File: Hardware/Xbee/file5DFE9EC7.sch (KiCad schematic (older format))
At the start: 36 parts, among them J1 Alimentación, J2 Raspberry, J3 Pines 1, J4 Pines 2, J5 Programación, J6 Entrada, J7 Salida, K1 SANYOU_SRD_Form_C, Q1 2N7002, Q2 AP2300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

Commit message: Sheets-Text
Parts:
- removed D1: Blue Assoc-RSSI, LED_SMD:LED_0805_2012Metric, symbol Xbee-rescue:LED_ALT-Device
- removed D3: Zener 5V, Diode_SMD:D_SOT-23_ANK, symbol Xbee-rescue:D_Zener_ALT-Device
- removed D4: 1N4007WS, Diode_SMD:D_SOD-323_HandSoldering, symbol Xbee-rescue:1N4007-Diode
- removed D5: LED ON, Connector_PinSocket_2.54mm:PinSocket_1x02_P2.54mm_Vertical, symbol Xbee-rescue:LED_ALT-Device
- removed D6: LED Batería, Connector_PinSocket_2.54mm:PinSocket_1x02_P2.54mm_Vertical, symbol Xbee-rescue:LED_ALT-Device
- removed D7: LED Green Salida, LED_SMD:LED_0805_2012Metric, symbol Xbee-rescue:LED_ALT-Device
- removed J1: Alimentación, TerminalBlock:TerminalBlock_bornier-2_P5.08mm, symbol Xbee-rescue:Screw_Terminal_01x02-Connector
- removed J2: Raspberry, Connector_PinHeader_2.54mm:PinHeader_1x05_P2.54mm_Vertical, symbol Xbee-rescue:Conn_01x05-Connector_Generic
- removed J3: Pines 1, Connector_PinSocket_2.54mm:PinSocket_1x10_P2.54mm_Vertical, symbol Xbee-rescue:Conn_01x10-Connector_Generic
- removed J4: Pines 2, Connector_PinSocket_2.54mm:PinSocket_1x10_P2.54mm_Vertical, symbol Xbee-rescue:Conn_01x10-Connector_Generic
- removed J5: Programación, Connector_PinHeader_2.54mm:PinHeader_2x05_P2.54mm_Horizontal, symbol Xbee-rescue:Conn_02x05_Counter_Clockwise-Connector_Generic
- removed J6: Entrada, TerminalBlock:TerminalBlock_bornier-2_P5.08mm, symbol Xbee-rescue:Screw_Terminal_01x02-Connector
- removed J7: Salida, TerminalBlock:TerminalBlock_bornier-2_P5.08mm, symbol Xbee-rescue:Screw_Terminal_01x02-Connector
- removed JP1: Assoc-RSSI, Connector_PinHeader_2.54mm:PinHeader_1x03_P2.54mm_Vertical, symbol Xbee-rescue:Jumper_3_Open-Jumper
- removed JP2: Loopback, Connector_PinHeader_2.54mm:PinHeader_1x02_P2.54mm_Vertical, symbol Xbee-rescue:Jumper_2_Open-Jumper
- removed JP3: DIO2 E/S, Connector_PinHeader_2.54mm:PinHeader_1x03_P2.54mm_Vertical, symbol Xbee-rescue:Jumper_3_Open-Jumper
- removed JP4: Estado Batería, Connector_PinHeader_2.54mm:PinHeader_1x02_P2.54mm_Vertical, symbol Xbee-rescue:Jumper_2_Open-Jumper
- removed K1: SANYOU_SRD_Form_C, Relay_THT:Relay_SPDT_SANYOU_SRD_Series_Form_C, symbol Relay:SANYOU_SRD_Form_C
- removed Q1: 2N7002, Package_TO_SOT_SMD:SOT-23, symbol Transistor_FET:2N7002
- removed Q2: AP2300, Package_TO_SOT_SMD:SOT-23, symbol Transistor_FET:2N7002
- removed R1, R5, R9: 330, Resistor_SMD:R_0805_2012Metric_Pad1.15x1.40mm_HandSolder, symbol Xbee-rescue:R-Device
- removed R10, R6, R8: 10k, Resistor_SMD:R_0805_2012Metric_Pad1.15x1.40mm_HandSolder, symbol Xbee-rescue:R-Device
- removed R11, R12: 560, Resistor_SMD:R_0805_2012Metric_Pad1.15x1.40mm_HandSolder, symbol Xbee-rescue:R-Device
- removed R13: 4k7, Resistor_SMD:R_0805_2012Metric_Pad1.15x1.40mm_HandSolder, symbol Xbee-rescue:R-Device
- removed R7: 3.3k, Resistor_SMD:R_0805_2012Metric_Pad1.15x1.40mm_HandSolder, symbol Xbee-rescue:R-Device
- removed RV1, RV2: 10k, Potentiometer_THT:Potentiometer_Bourns_3386C_Horizontal, symbol Xbee-rescue:R_POT-Device
- removed SW1: Reset, Button_Switch_THT:SW_TH_Tactile_Omron_B3F-10xx, symbol Xbee-rescue:SW_Push_Dual-Switch
- removed SW2: Comm., Button_Switch_THT:SW_TH_Tactile_Omron_B3F-10xx, symbol Xbee-rescue:SW_Push_Dual-Switch
- removed U2: Xbee, XBP24CZ7PITB003:DIP2200W51P200L3294H279Q20P, symbol Xbee-rescue:XBP24CZ7PITB003-XBP24CZ7PITB003
- removed U3: LM358, Package_SO:SO-8_3.9x4.9mm_P1.27mm, symbol Xbee-rescue:LM358-Amplifier_Operational
- added C1, C2: 1u, Capacitor_SMD:C_0805_2012Metric, symbol Xbee-rescue:CP1-Device
- added U1: AZ1117-3.3, Package_TO_SOT_SMD:SOT-223-3_TabPin2, symbol Regulator_Linear:AZ1117-3.3
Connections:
- net GNDREF: now also C1.2, C2.2, U1.1 (GND)
- new net Entrada-12V: C1.1, U1.3 (VI)
- new net Salida-3.3V: C2.1, U1.2 (VO)
- no-connect marks 6 -> 0
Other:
- note added: "Regulador-3.3V"
- note removed: "Borneras-Entrada-Salida"
- note removed: "Botones"
- note removed: "Circuito-Salida"
- note removed: "Estado-Batería"
- note removed: "Jumper-Prog"
- note removed: "LED's Indicadores"
- note removed: "Lectura-Estado-Bateria"

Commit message: Battery Charger
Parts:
- added D2, D9: D_Schottky_ALT, symbol Device:D_Schottky_ALT
- added D8: D_ALT, symbol Device:D_ALT
- added Q3: DMP3099L-7, Package_TO_SOT_SMD:SOT-23, symbol Transistor_FET:DMP3013SFV
- added R2: 100, symbol Device:R
- added R3: 10k, symbol Device:R
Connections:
- net labels added: +12V, Bat+, CargaBat, Vin+
- wire segments 9 -> 23
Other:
- note added: "Cargador de batería"
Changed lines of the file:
@@
 EndData
 $EndBitmap
+Text HLabel 6000 1350 1    50   Input ~ 0
+Vin+
+Text HLabel 4700 2250 0    50   Input ~ 0
+Bat+
+$Comp
+L Device:D_Schottky_ALT D2
+U 1 1 5D952A15
+P 4750 1500
+F 0 "D2" H 4750 1716 50  0000 C CNN
+F 1 "D_Schottky_ALT" H 4750 1625 50  0000 C CNN
+F 2 "" H 4750 1500 50  0001 C CNN
+F 3 "~" H 4750 1500 50  0001 C CNN
+	1    4750 1500
+	0    -1   -1   0
+$EndComp
+$Comp
+L Device:D_ALT D8
+U 1 1 5D952EF8
+P 5800 2250
+F 0 "D8" H 5800 2034 50  0000 C CNN
+F 1 "D_ALT" H 5800 2125 50  0000 C CNN
+F 2 "" H 5800 2250 50  0001 C CNN
+F 3 "~" H 5800 2250 50  0001 C CNN
+	1    5800 2250
+	-1   0    0    1
+$EndComp
+$Comp
+L Device:R R3
+U 1 1 5D9533C4
+P 5600 1500
+F 0 "R3" H 5670 1546 50  0000 L CNN
+F 1 "10k" H 5670 1455 50  0000 L CNN
+F 2 "" V 5530 1500 50  0001 C CNN
+F 3 "~" H 5600 1500 50  0001 C CNN
+	1    5600 1500
+	1    0    0    -1
+$EndComp
+Wire Wire Line
+	5300 1350 5600 1350
+Wire Wire Line
+	5100 1650 5400 1650
+Wire Wire Line
+	6000 1350 5600 1350
+Connection ~ 5600 1350
+$Comp
+L Device:D_Schottky_ALT D9
+U 1 1 5D9575F1
+P 6000 1750
+F 0 "D9" V 6046 1671 50  0000 R CNN
+F 1 "D_Schottky_ALT" V 5955 1671 50  0000 R CNN
+F 2 "" H 6000 1750 50  0001 C CNN
+F 3 "~" H 6000 1750 50  0001 C CNN
+	1    6000 1750
+	0    -1   -1   0
+$EndComp
+Wire Wire Line
+	6000 1600 6000 1350
+$Comp
+L power:+12V #PWR0103
+U 1 1 5D9587BC
+P 6250 2250
+F 0 "#PWR0103" H 6250 2100 50  0001 C CNN
+F 1 "+12V" H 6265 2423 50  0000 C CNN
+F 2 "" H 6250 2250 50  0001 C CNN
+F 3 "" H 6250 2250 50  0001 C CNN
+	1    6250 2250
+	1    0    0    -1
+$EndComp
+$Comp
+L Device:R R2
+U 1 1 5D95A68D
+P 4750 1900
+F 0 "R2" V 4543 1900 50  0000 C CNN
+F 1 "100" V 4634 1900 50  0000 C CNN
+F 2 "" V 4680 1900 50  0001 C CNN
+F 3 "~" H 4750 1900 50  0001 C CNN
+	1    4750 1900
+	1    0    0    -1
+$EndComp
+Wire Wire Line
+	6000 1900 6000 2250
+Wire Wire Line
+	5950 2250 6000 2250
+Connection ~ 6000 2250
+Wire Wire Line
+	6000 2250 6250 2250
+Wire Wire Line
+	4750 1350 4900 1350
+Wire Wire Line
+	4750 1650 4750 1750
+Wire Wire Line
+	4750 2050 4750 2250
+Wire Wire Line
+	4750 2250 5650 2250
+Wire Wire Line
+	4700 2250 4750 2250
+Connection ~ 4750 2250
+Text HLabel 5400 1950 0    50   Input ~ 0
+CargaBat
+Wire Wire Line
+	5400 1950 5400 1650
+Connection ~ 5400 1650
+Wire Wire Line
+	5400 1650 5600 1650
+Text Notes 4800 950  0    79   ~ 0
+Cargador de batería
+$Comp
+L Transistor_FET:DMP3013SFV Q3
+U 1 1 5DAEF0EF
+P 5100 1450
+F 0 "Q3" V 5443 1450 50  0000 C CNN
+F 1 "DMP3099L-7" V 5352 1450 50  0000 C CNN
+F 2 "Package_TO_SOT_SMD:SOT-23" H 5300 1375 50  0001 L CIN
+F 3 "https://www.diodes.com/assets/Datasheets/DMP3013SFV.pdf" V 5100 1450 50  0001 L CNN
+	1    5100 1450
+	0    -1   -1   0
+$EndComp
 $EndSCHEMATC

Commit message: Added Diodes Footprints
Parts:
- D2, D9: value D_Schottky_ALT -> DSU24; footprint (none) -> Diode_SMD:D_SOD-123
- D8: value D_ALT -> DSK26; footprint (none) -> Diode_SMD:D_SOD-123F
- R2: footprint (none) -> Resistor_SMD:R_2512_6332Metric_Pad1.52x3.35mm_HandSolder
- R3: footprint (none) -> Resistor_SMD:R_0805_2012Metric_Pad1.15x1.40mm_HandSolder
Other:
- moved on the sheet: D2, D8, D9, R2, R3
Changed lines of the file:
@@
 EndData
 $EndBitmap
-Text HLabel 6000 1350 1    50   Input ~ 0
+Text HLabel 5850 1450 1    50   Input ~ 0
 Vin+
-Text HLabel 4700 2250 0    50   Input ~ 0
+Text HLabel 4550 2350 0    50   Input ~ 0
 Bat+
 $Comp
 L Device:D_Schottky_ALT D2
 U 1 1 5D952A15
-P 4750 1500
-F 0 "D2" H 4750 1716 50  0000 C CNN
-F 1 "D_Schottky_ALT" H 4750 1625 50  0000 C CNN
-F 2 "" H 4750 1500 50  0001 C CNN
-F 3 "~" H 4750 1500 50  0001 C CNN
-	1    4750 1500
+P 4600 1600
+F 0 "D2" H 4600 1816 50  0000 C CNN
+F 1 "DSU24" H 4600 1725 50  0000 C CNN
+F 2 "Diode_SMD:D_SOD-123" H 4600 1600 50  0001 C CNN
+F 3 "~" H 4600 1600 50  0001 C CNN
+	1    4600 1600
 	0    -1   -1   0
 $EndComp
@@
 L Device:D_ALT D8
 U 1 1 5D952EF8
-P 5800 2250
-F 0 "D8" H 5800 2034 50  0000 C CNN
-F 1 "D_ALT" H 5800 2125 50  0000 C CNN
-F 2 "" H 5800 2250 50  0001 C CNN
-F 3 "~" H 5800 2250 50  0001 C CNN
-	1    5800 2250
+P 5650 2350
+F 0 "D8" H 5650 2134 50  0000 C CNN
+F 1 "DSK26" H 5650 2225 50  0000 C CNN
+F 2 "Diode_SMD:D_SOD-123F" H 5650 2350 50  0001 C CNN
+F 3 "~" H 5650 2350 50  0001 C CNN
+	1    5650 2350
 	-1   0    0    1
 $EndComp
@@
 L Device:R R3
 U 1 1 5D9533C4
-P 5600 1500
-F 0 "R3" H 5670 1546 50  0000 L CNN
-F 1 "10k" H 5670 1455 50  0000 L CNN
-F 2 "" V 5530 1500 50  0001 C CNN
-F 3 "~" H 5600 1500 50  0001 C CNN
-	1    5600 1500
+P 5450 1600
+F 0 "R3" H 5520 1646 50  0000 L CNN
+F 1 "10k" H 5520 1555 50  0000 L CNN
+F 2 "Resistor_SMD:R_0805_2012Metric_Pad1.15x1.40mm_HandSolder" V 5380 1600 50  0001 C CNN
+F 3 "~" H 5450 1600 50  0001 C CNN
+	1    5450 1600
 	1    0    0    -1
 $EndComp
 Wire Wire Line
-	5300 1350 5600 1350
+	5150 1450 5450 1450
 Wire Wire Line
-	5100 1650 5400 1650
+	4950 1750 5250 1750
 Wire Wire Line
-	6000 1350 5600 1350
-Connection ~ 5600 1350
+	5850 1450 5450 1450
+Connection ~ 5450 1450
 $Comp
 L Device:D_Schottky_ALT D9
 U 1 1 5D9575F1
-P 6000 1750
-F 0 "D9" V 6046 1671 50  0000 R CNN
-F 1 "D_Schottky_ALT" V 5955 1671 50  0000 R CNN
-F 2 "" H 6000 1750 50  0001 C CNN
-F 3 "~" H 6000 1750 50  0001 C CNN
-	1    6000 1750
+P 5850 1850
+F 0 "D9" V 5896 1771 50  0000 R CNN
+F 1 "DSU24" V 5805 1771 50  0000 R CNN
+F 2 "Diode_SMD:D_SOD-123" H 5850 1850 50  0001 C CNN
+F 3 "~" H 5850 1850 50  0001 C CNN
+	1    5850 1850
 	0    -1   -1   0
 $EndComp
 Wire Wire Line
-	6000 1600 6000 1350
+	5850 1700 5850 1450
 $Comp
 L power:+12V #PWR0103
 U 1 1 5D9587BC
-P 6250 2250
-F 0 "#PWR0103" H 6250 2100 50  0001 C CNN
-F 1 "+12V" H 6265 2423 50  0000 C CNN
-F 2 "" H 6250 2250 50  0001 C CNN
-F 3 "" H 6250 2250 50  0001 C CNN
-	1    6250 2250
+P 6100 2350
+F 0 "#PWR0103" H 6100 2200 50  0001 C CNN
+F 1 "+12V" H 6115 2523 50  0000 C CNN
+F 2 "" H 6100 2350 50  0001 C CNN
+F 3 "" H 6100 2350 50  0001 C CNN
+	1    6100 2350
 	1    0    0    -1
 $EndComp
@@
 L Device:R R2
 U 1 1 5D95A68D
-P 4750 1900
-F 0 "R2" V 4543 1900 50  0000 C CNN
-F 1 "100" V 4634 1900 50  0000 C CNN
-F 2 "" V 4680 1900 50  0001 C CNN
-F 3 "~" H 4750 1900 50  0001 C CNN
-	1    4750 1900
+P 4600 2000
+F 0 "R2" V 4393 2000 50  0000 C CNN
+F 1 "100" V 4484 2000 50  0000 C CNN
+F 2 "Resistor_SMD:R_2512_6332Metric_Pad1.52x3.35mm_HandSolder" V 4530 2000 50  0001 C CNN
+F 3 "~" H 4600 2000 50  0001 C CNN
+	1    4600 2000
 	1    0    0    -1
 $EndComp
 Wire Wire Line
-	6000 1900 6000 2250
+	5850 2000 5850 2350
 Wire Wire Line
-	5950 2250 6000 2250
-Connection ~ 6000 2250
+	5800 2350 5850 2350
+Connection ~ 5850 2350
 Wire Wire Line
-	6000 2250 6250 2250
+	5850 2350 6100 2350
 Wire Wire Line
-	4750 1350 4900 1350
+	4600 1450 4750 1450
 Wire Wire Line
-	4750 1650 4750 1750
+	4600 1750 4600 1850
 Wire Wire Line
-	4750 2050 4750 2250
+	4600 2150 4600 2350
 Wire Wire Line
-	4750 2250 5650 2250
+	4600 2350 5500 2350
 Wire Wire Line
-	4700 2250 4750 2250
-Connection ~ 4750 2250
-Text HLabel 5400 1950 0    50   Input ~ 0
+	4550 2350 4600 2350
+Connection ~ 4600 2350
+Text HLabel 5250 2050 0    50   Input ~ 0
 CargaBat
 Wire Wire Line
-	5400 1950 5400 1650
-Connection ~ 5400 1650
+	5250 2050 5250 1750
+Connection ~ 5250 1750
 Wire Wire Line
-	5400 1650 5600 1650
-Text Notes 4800 950  0    79   ~ 0
+	5250 1750 5450 1750
+Text Notes 4650 1050 0    79   ~ 0
 Cargador de batería
 $Comp
 L Transistor_FET:DMP3013SFV Q3
 U 1 1 5DAEF0EF
-P 5100 1450
-F 0 "Q3" V 5443 1450 50  0000 C CNN
-F 1 "DMP3099L-7" V 5352 1450 50  0000 C CNN
-F 2 "Package_TO_SOT_SMD:SOT-23" H 5300 1375 50  0001 L CIN
-F 3 "https://www.diodes.com/assets/Datasheets/DMP3013SFV.pdf" V 5100 1450 50  0001 L CNN
-	1    5100 1450
+P 4950 1550
+F 0 "Q3" V 5293 1550 50  0000 C CNN
+F 1 "DMP3099L-7" V 5202 1550 50  0000 C CNN
+F 2 "Package_TO_SOT_SMD:SOT-23" H 5150 1475 50  0001 L CIN
+F 3 "https://www.diodes.com/assets/Datasheets/DMP3013SFV.pdf" V 4950 1550 50  0001 L CNN
+	1    4950 1550
 	0    -1   -1   0
 $EndComp
+Wire Notes Line
+	3850 850  6400 850
+Wire Notes Line
+	6400 850  6400 2500
+Wire Notes Line
+	3850 2500 3850 850
+Wire Notes Line
+	3850 2500 6400 2500
 $EndSCHEMATC

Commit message: PCB Component Placement
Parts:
- removed Q3: DMP3099L-7, Package_TO_SOT_SMD:SOT-23, symbol Transistor_FET:DMP3013SFV
- added Q3: DMP3099L-7, Package_TO_SOT_SMD:SOT-23, symbol Device:Q_PMOS_GSD
- C1, C2: footprint Capacitor_SMD:C_0805_2012Metric -> Capacitor_SMD:C_0805_2012Metric_Pad1.15x1.40mm_HandSolder
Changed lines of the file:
@@
 F 0 "C1" H 1665 1896 50  0000 L CNN
 F 1 "1u" H 1665 1805 50  0000 L CNN
-F 2 "Capacitor_SMD:C_0805_2012Metric" H 1550 1850 50  0001 C CNN
+F 2 "Capacitor_SMD:C_0805_2012Metric_Pad1.15x1.40mm_HandSolder" H 1550 1850 50  0001 C CNN
 F 3 "~" H 1550 1850 50  0001 C CNN
 	1    1550 1850
@@
 F 0 "C2" H 3015 1896 50  0000 L CNN
 F 1 "1u" H 3015 1805 50  0000 L CNN
-F 2 "Capacitor_SMD:C_0805_2012Metric" H 2900 1850 50  0001 C CNN
+F 2 "Capacitor_SMD:C_0805_2012Metric_Pad1.15x1.40mm_HandSolder" H 2900 1850 50  0001 C CNN
 F 3 "~" H 2900 1850 50  0001 C CNN
 	1    2900 1850
@@
 Text Notes 4650 1050 0    79   ~ 0
 Cargador de batería
-$Comp
-L Transistor_FET:DMP3013SFV Q3
-U 1 1 5DAEF0EF
-P 4950 1550
-F 0 "Q3" V 5293 1550 50  0000 C CNN
-F 1 "DMP3099L-7" V 5202 1550 50  0000 C CNN
-F 2 "Package_TO_SOT_SMD:SOT-23" H 5150 1475 50  0001 L CIN
-F 3 "https://www.diodes.com/assets/Datasheets/DMP3013SFV.pdf" V 4950 1550 50  0001 L CNN
-	1    4950 1550
-	0    -1   -1   0
-$EndComp
 Wire Notes Line
 	3850 850  6400 850
@@
 Wire Notes Line
 	3850 2500 6400 2500
+$Comp
+L Device:Q_PMOS_GSD Q3
+U 1 1 5D9BD611
+P 4950 1550
+F 0 "Q3" V 5293 1550 50  0000 C CNN
+F 1 "DMP3099L-7" V 5202 1550 50  0000 C CNN
+F 2 "Package_TO_SOT_SMD:SOT-23" H 5150 1650 50  0001 C CNN
+F 3 "~" H 4950 1550 50  0001 C CNN
+	1    4950 1550
+	0    -1   -1   0
+$EndComp
 $EndSCHEMATC

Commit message: PCB Component placement
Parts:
- R2: footprint Resistor_SMD:R_2512_6332Metric_Pad1.52x3.35mm_HandSolder -> Resistor_SMD:R_1218_3246Metric_Pad1.22x4.75mm_HandSolder
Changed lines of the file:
@@
 F 0 "R2" V 4393 2000 50  0000 C CNN
 F 1 "100" V 4484 2000 50  0000 C CNN
-F 2 "Resistor_SMD:R_2512_6332Metric_Pad1.52x3.35mm_HandSolder" V 4530 2000 50  0001 C CNN
+F 2 "Resistor_SMD:R_1218_3246Metric_Pad1.22x4.75mm_HandSolder" V 4530 2000 50  0001 C CNN
 F 3 "~" H 4600 2000 50  0001 C CNN
 	1    4600 2000

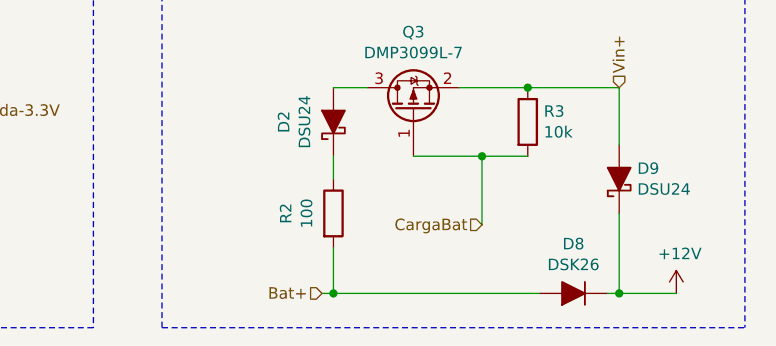
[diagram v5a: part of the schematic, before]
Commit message: Add Fuse
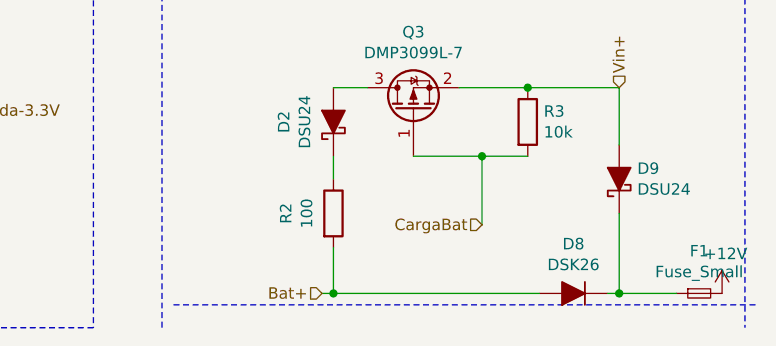
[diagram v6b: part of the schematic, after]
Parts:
- added F1: Fuse_Small, Fuse:Fuse_1206_3216Metric_Pad1.42x1.75mm_HandSolder, symbol Device:Fuse_Small
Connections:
- net +12V: now also F1.2; no longer D8.1 (K), D9.1 (K)
- new net: D8.1 (K), D9.1 (K), F1.1
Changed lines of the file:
@@
 L power:+12V #PWR0103
 U 1 1 5D9587BC
-P 6100 2350
-F 0 "#PWR0103" H 6100 2200 50  0001 C CNN
-F 1 "+12V" H 6115 2523 50  0000 C CNN
-F 2 "" H 6100 2350 50  0001 C CNN
-F 3 "" H 6100 2350 50  0001 C CNN
-	1    6100 2350
+P 6300 2350
+F 0 "#PWR0103" H 6300 2200 50  0001 C CNN
+F 1 "+12V" H 6315 2523 50  0000 C CNN
+F 2 "" H 6300 2350 50  0001 C CNN
+F 3 "" H 6300 2350 50  0001 C CNN
+	1    6300 2350
 	1    0    0    -1
 $EndComp
@@
 	3850 2500 3850 850
 Wire Notes Line
-	3850 2500 6400 2500
+	3900 2400 6450 2400
 $Comp
 L Device:Q_PMOS_GSD Q3
@@
 	0    -1   -1   0
 $EndComp
+$Comp
+L Device:Fuse_Small F1
+U 1 1 5DA124EC
+P 6200 2350
+F 0 "F1" H 6200 2535 50  0000 C CNN
+F 1 "Fuse_Small" H 6200 2444 50  0000 C CNN
+F 2 "Fuse:Fuse_1206_3216Metric_Pad1.42x1.75mm_HandSolder" H 6200 2350 50  0001 C CNN
+F 3 "~" H 6200 2350 50  0001 C CNN
+	1    6200 2350
+	1    0    0    -1
+$EndComp
 $EndSCHEMATC

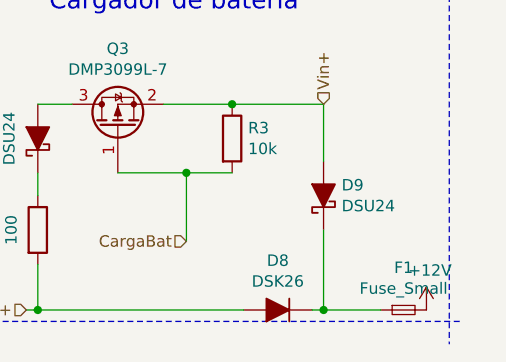
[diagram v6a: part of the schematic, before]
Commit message: Localización de componentes
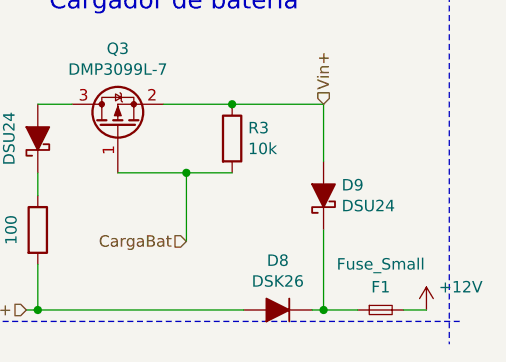
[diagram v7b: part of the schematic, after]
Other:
- moved on the sheet: F1
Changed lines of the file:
@@
 EESchema Schematic File Version 4
 LIBS:Xbee-cache
-EELAYER 30 0
+EELAYER 29 0
 EELAYER END
 $Descr A4 11693 8268
@@
 P 6300 2350
 F 0 "#PWR0103" H 6300 2200 50  0001 C CNN
-F 1 "+12V" H 6315 2523 50  0000 C CNN
+F 1 "+12V" H 6450 2450 50  0000 C CNN
 F 2 "" H 6300 2350 50  0001 C CNN
 F 3 "" H 6300 2350 50  0001 C CNN
@@
 Wire Wire Line
 	5800 2350 5850 2350
-Connection ~ 5850 2350
-Wire Wire Line
-	5850 2350 6100 2350
 Wire Wire Line
 	4600 1450 4750 1450
@@
 L Device:Fuse_Small F1
 U 1 1 5DA124EC
-P 6200 2350
-F 0 "F1" H 6200 2535 50  0000 C CNN
-F 1 "Fuse_Small" H 6200 2444 50  0000 C CNN
-F 2 "Fuse:Fuse_1206_3216Metric_Pad1.42x1.75mm_HandSolder" H 6200 2350 50  0001 C CNN
-F 3 "~" H 6200 2350 50  0001 C CNN
-	1    6200 2350
+P 6100 2350
+F 0 "F1" H 6100 2450 50  0000 C CNN
+F 1 "Fuse_Small" H 6100 2550 50  0000 C CNN
+F 2 "Fuse:Fuse_1206_3216Metric_Pad1.42x1.75mm_HandSolder" H 6100 2350 50  0001 C CNN
+F 3 "~" H 6100 2350 50  0001 C CNN
+	1    6100 2350
 	1    0    0    -1
 $EndComp
+Wire Wire Line
+	6200 2350 6300 2350
+Wire Wire Line
+	6000 2350 5850 2350
+Connection ~ 5850 2350
 $EndSCHEMATC
